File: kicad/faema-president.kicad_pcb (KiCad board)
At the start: 2 copper layers, 90 x 80 mm, 43 parts, among them J1 AC_INPUT_220V, J10 SSR_CTRL_HEADER, J2 AC_BOILER_OUT, J3 PT100_CALDEIRA, J5 ILI9341_2.4_HEADER, J6 PT100_GRUPO, J7 SONDA_NIVEL, J8 BOTOES_PRESET, J9 ENCODER_EC11, Q1 2N7002, U1 ESP32-S3-MINI-1-N8, U2 HLK-PM05, U3 AMS1117-3.3, U4 MAX31865_CALDEIRA, U5 DS3231SN, U6 MAX31865_GRUPO

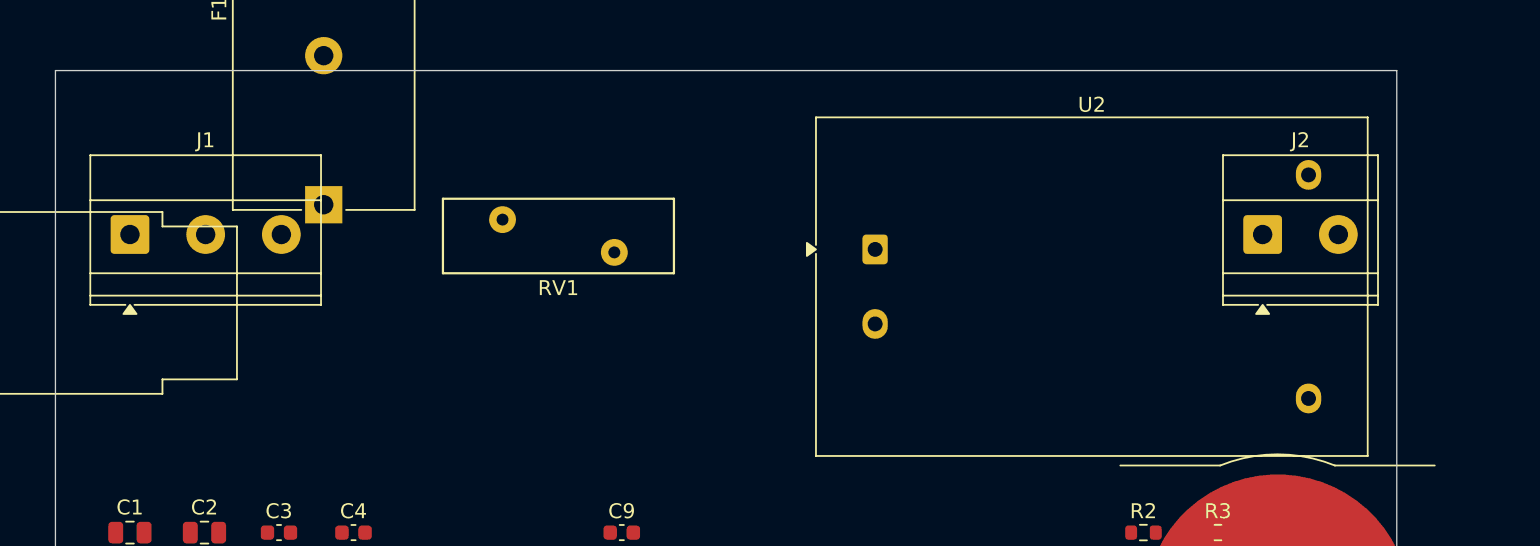
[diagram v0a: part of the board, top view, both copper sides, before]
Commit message: Remover F1/F2 da PCB: fusíveis ficam em porta-fusível de painel externo
- F1, F2 (T16A slow-blow) removidos do circuito SKiDL
- Nets AC_L1/AC_L2 pré-fusível removidas
- J1 recebe L1_fused e L2_fused diretamente (já fusadas externamente)
- Zona AC da placa: apenas J1 + RV1 + U2 (~81mm) → cabe em 90mm
- place_components.py: F1/F2 removidos, J1/RV1/U2 reposicionados

Co-Authored-By: Claude Sonnet 4.6 <noreply@anthropic.com>
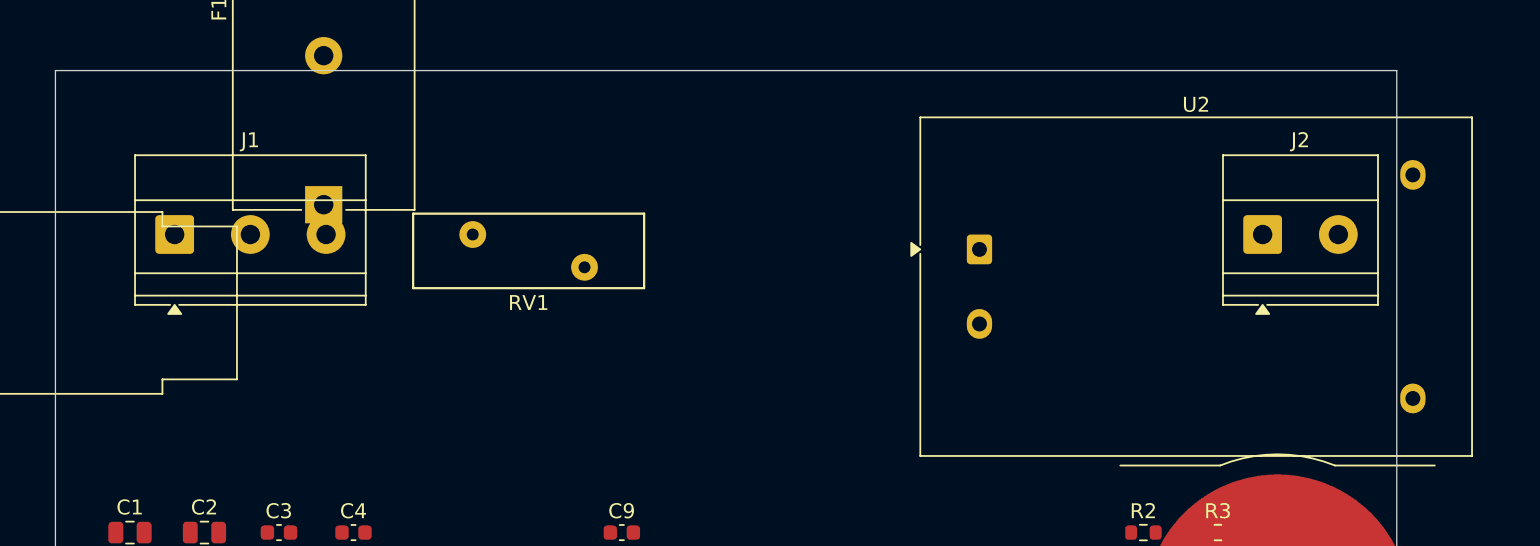
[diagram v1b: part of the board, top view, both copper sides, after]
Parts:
- moved U2 7.00 mm to (112.0, 62.0)
- moved J1 3.00 mm to (58.0, 61.0)
- moved RV1 2.24 mm to (78.0, 61.0)
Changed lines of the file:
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@@
 	(footprint "Varistor:RV_Disc_D15.5mm_W5mm_P7.5mm"
 		(layer "F.Cu")
-		(at 80 60)
+		(at 78 61)
 		(descr "Varistor, diameter 15.5mm, width 5mm, pitch 7.5mm")
 		(tags "varistor SIOV")
@@
 	(footprint "TerminalBlock_Phoenix:TerminalBlock_Phoenix_MKDS-1,5-3-5.08_1x03_P5.08mm_Horizontal"
 		(layer "F.Cu")
-		(at 55 61)
+		(at 58 61)
 		(descr "Terminal Block Phoenix MKDS-1,5-3-5.08, 3 pins, pitch 5.08mm, size 15.2x9.8mm, drill diameter 1.3mm, pad diameter 2.6mm, http://www.farnell.com/datasheets/100425.pdf")
 		(tags "THT Terminal Block Phoenix MKDS-1,5-3-5.08 pitch 5.08mm size 15.2x9.8mm drill 1.3mm pad 2.6mm")
@@
 	(footprint "Converter_ACDC:Converter_ACDC_Hi-Link_HLK-PMxx"
 		(layer "F.Cu")
-		(at 105 62)
+		(at 112 62)
 		(descr "ACDC-Converter, 3W, Hi-Link, HLK-PMxx, THT, https://h.hlktech.com/download/ACDC%E7%94%B5%E6%BA%90%E6%A8%A1%E5%9D%973W%E7%B3%BB%E5%88%97/1/%E6%B5%B7%E5%87%8C%E7%A7%913W%E7%B3%BB%E5%88%97%E7%94%B5%E6%BA%90%E6%A8%A1%E5%9D%97%E8%A7%84%E6%A0%BC%E4%B9%A6V2.8.pdf")
 		(tags "ACDC-Converter 3W THT Hi-Link board mount module")

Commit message: Rev.6: carrier board SKiDL + limpeza do repositório
- circuits/faema_carrier.py: novo circuito SKiDL para carrier board
  (Pico 2W + 3× SEN-30201 RTD breakouts + Nextion UART)
- outputs/faema_carrier.net: netlist gerada (0 erros ERC)
- SPEC.md: reescrito para Rev.6 carrier board architecture
- .gitignore: adiciona padrões SKiDL, Python cache, .DS_Store, Gerbers
- clean.sh: script para remover arquivos temporários recorrentes
- Remove HTMLs obsoletos do Rev.4/5 (president_schematic_v2/v3.html)
- outputs/bom_jlcpcb.csv, cpl_jlcpcb.csv: outputs JLCPCB do Rev.4/5

Co-Authored-By: Claude Sonnet 4.6 <noreply@anthropic.com>
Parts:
- removed F1, F2: T16A_SLOW, Fuse:Fuseholder_Cylinder-5x20mm_Schurter_FAB_0031-355x_Horizontal_Closed
- removed J2: AC_BOILER_OUT, TerminalBlock_Phoenix:TerminalBlock_Phoenix_MKDS-1,5-2-5.08_1x02_P5.08mm_Horizontal
- moved J10 43.0 mm to (73.9, 91.5)
- moved J6 34.7 mm to (79.5, 102.4)
- moved J5 27.4 mm to (120.0, 108.5)
- moved J7 20.6 mm to (105.5, 124.0)
- moved U5 20.4 mm to (110.3, 107.6)
- moved J8 19.5 mm to (128.5, 113.0)
- moved J9 14.5 mm to (136.0, 115.5)
- moved BT1 12.9 mm to (119.7, 90.0)
- moved U6 11.5 mm to (81.5, 123.5)
- moved U1 11.4 mm to (93.8, 98.0)
- moved U2 9.63 mm to (102.4, 61.0)
- moved U4 2.92 mm to (72.5, 114.5)
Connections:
- J1 pad 1: AC_L1 -> AC_L1_FUSED
- J1 pad 2: AC_L2 -> AC_L2_FUSED
